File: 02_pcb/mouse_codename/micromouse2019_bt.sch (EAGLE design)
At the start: 2 parts, among them U1 SPBT2632C2A.AT2

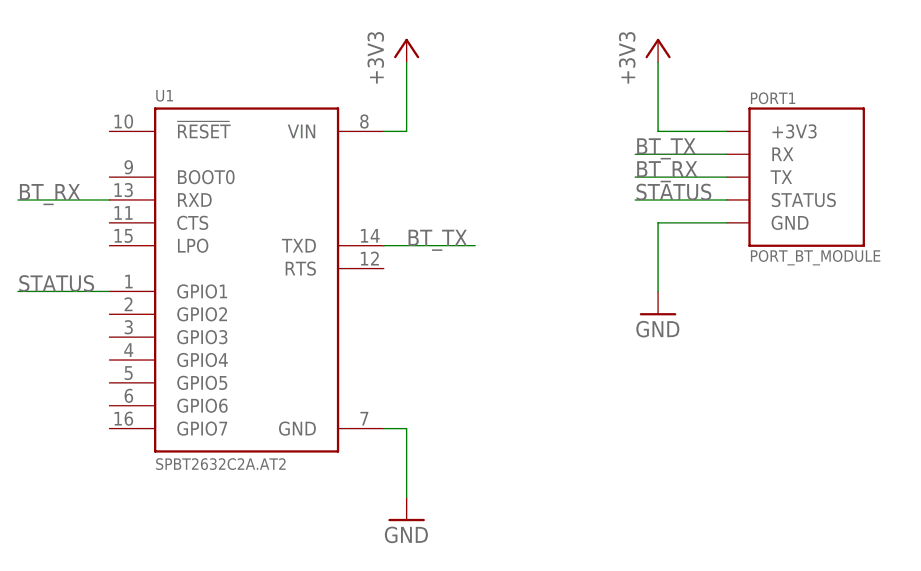
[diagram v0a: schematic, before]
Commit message: bt_port tx rx changed
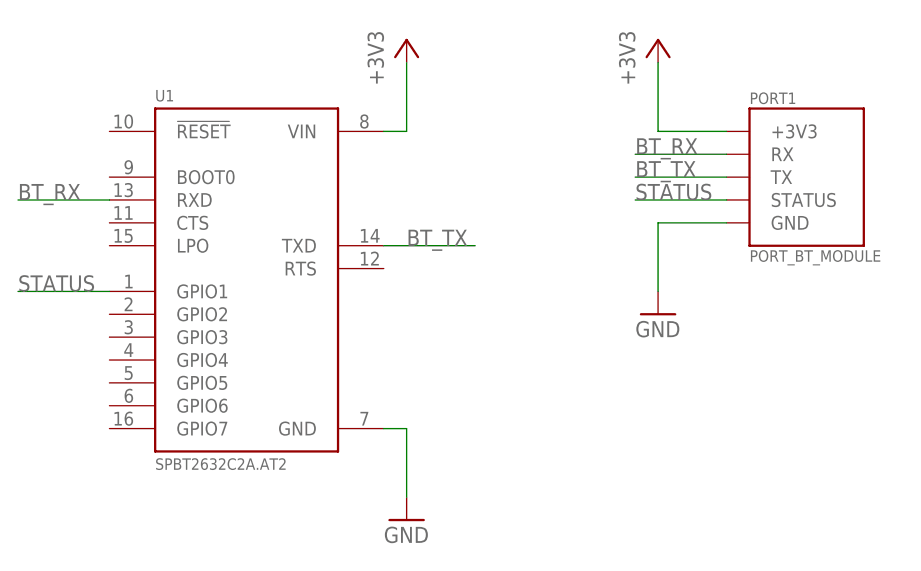
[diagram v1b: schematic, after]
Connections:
- net BT_RX: now also PORT1.RX; no longer PORT1.TX
- net BT_TX: now also PORT1.TX; no longer PORT1.RX
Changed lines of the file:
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@@
 </segment>
 <segment>
-<pinref part="PORT1" gate="G$1" pin="RX"/>
-<wire x1="53.34" y1="12.7" x2="43.18" y2="12.7" width="0.1524" layer="91"/>
-<label x="43.18" y="12.7" size="1.778" layer="95"/>
+<pinref part="PORT1" gate="G$1" pin="TX"/>
+<wire x1="53.34" y1="10.16" x2="43.18" y2="10.16" width="0.1524" layer="91"/>
+<label x="43.18" y="10.16" size="1.778" layer="95"/>
 </segment>
 </net>
@@
 </segment>
 <segment>
-<pinref part="PORT1" gate="G$1" pin="TX"/>
-<wire x1="53.34" y1="10.16" x2="43.18" y2="10.16" width="0.1524" layer="91"/>
-<label x="43.18" y="10.16" size="1.778" layer="95"/>
+<pinref part="PORT1" gate="G$1" pin="RX"/>
+<wire x1="53.34" y1="12.7" x2="43.18" y2="12.7" width="0.1524" layer="91"/>
+<label x="43.18" y="12.7" size="1.778" layer="95"/>
 </segment>
 </net>
